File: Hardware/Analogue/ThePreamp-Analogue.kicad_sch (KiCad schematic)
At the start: 32 parts, among them IC1 ULN2803CDWR, J1 To preamp, J14 Conn_01x03_Pin, J15 Conn_02x06_Top_Bottom, J2 From preamp, J3 Digital In, J4 Digital Pass Through, J5 Power In, J6 Power Out, J7 ADS1115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

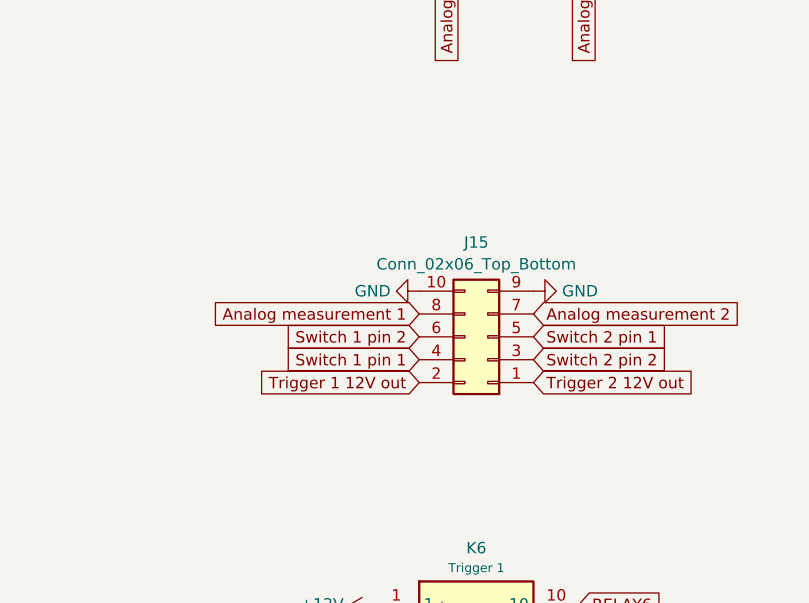
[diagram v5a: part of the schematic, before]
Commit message: Changed switch connector to 1 row
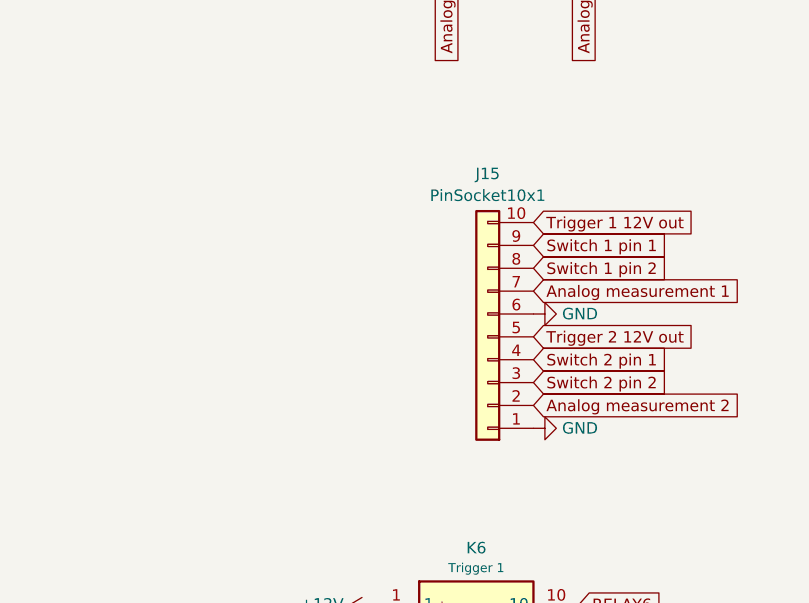
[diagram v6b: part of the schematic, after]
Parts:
- J15: value Conn_02x06_Top_Bottom -> PinSocket10x1; footprint Connector_IDC:IDC-Header_2x05_P2.54mm_Vertical -> Connector_PinSocket_2.54mm:PinSocket_1x10_P2.54mm_Vertical; symbol Connector_Generic:Conn_02x05_Odd_Even -> Connector_Generic:Conn_01x10
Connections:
- net A0: now also J15.7 (Pin_7); no longer J15.8 (Pin_8)
- net A1: now also J15.2 (Pin_2); no longer J15.7 (Pin_7)
- net GND: now also J15.1 (Pin_1), J15.6 (Pin_6); no longer J15.10 (Pin_10), J15.9 (Pin_9)
- net Switch 1 pin 1: now also J15.9 (Pin_9); no longer J15.4 (Pin_4)
- net Switch 1 pin 2: now also J15.8 (Pin_8); no longer J15.6 (Pin_6)
- net Switch 2 pin 1: now also J15.4 (Pin_4); no longer J15.5 (Pin_5)
- net Trigger 1 12V out: now also J15.10 (Pin_10); no longer J15.2 (Pin_2)
- net Trigger 2 12V out: now also J15.5 (Pin_5); no longer J15.1 (Pin_1)
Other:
- moved on the sheet: J15
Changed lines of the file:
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@@
     )
   )
-  (global_label "Analog measurement 2" (shape input) (at 354.076 118.11 0) (fields_autoplaced)
-    (effects (font (size 1.27 1.27)) (justify left))
-    (property "Intersheetrefs" "${INTERSHEET_REFS}" (at 378.5409 118.11 0)
+  (global_label "Analog measurement 2" (shape input) (at 354.076 128.27 0) (fields_autoplaced)
+    (effects (font (size 1.27 1.27)) (justify left))
+    (property "Intersheetrefs" "${INTERSHEET_REFS}" (at 378.5409 128.27 0)
       (effects (font (size 1.27 1.27)) (justify left) hide)
     )
@@
     )
   )
-  (global_label "Switch 1 pin 1" (shape input) (at 341.376 123.19 180) (fields_autoplaced)
-    (effects (font (size 1.27 1.27)) (justify right))
-    (property "Intersheetrefs" "${INTERSHEET_REFS}" (at 324.7123 123.19 0)
-      (effects (font (size 1.27 1.27)) (justify right) hide)
+  (global_label "Switch 1 pin 1" (shape input) (at 354.076 110.49 0) (fields_autoplaced)
+    (effects (font (size 1.27 1.27)) (justify left))
+    (property "Intersheetrefs" "${INTERSHEET_REFS}" (at 370.7397 110.49 0)
+      (effects (font (size 1.27 1.27)) (justify left) hide)
     )
   )
@@
     )
   )
-  (global_label "Trigger 2 12V out" (shape input) (at 354.076 125.73 0) (fields_autoplaced)
-    (effects (font (size 1.27 1.27)) (justify left))
-    (property "Intersheetrefs" "${INTERSHEET_REFS}" (at 373.582 125.73 0)
+  (global_label "Trigger 2 12V out" (shape input) (at 354.076 120.65 0) (fields_autoplaced)
+    (effects (font (size 1.27 1.27)) (justify left))
+    (property "Intersheetrefs" "${INTERSHEET_REFS}" (at 373.582 120.65 0)
       (effects (font (size 1.27 1.27)) (justify left) hide)
     )
@@
     )
   )
-  (global_label "Trigger 1 12V out" (shape input) (at 341.376 125.73 180) (fields_autoplaced)
-    (effects (font (size 1.27 1.27)) (justify right))
-    (property "Intersheetrefs" "${INTERSHEET_REFS}" (at 321.87 125.73 0)
-      (effects (font (size 1.27 1.27)) (justify right) hide)
+  (global_label "Trigger 1 12V out" (shape input) (at 354.076 107.95 0) (fields_autoplaced)
+    (effects (font (size 1.27 1.27)) (justify left))
+    (property "Intersheetrefs" "${INTERSHEET_REFS}" (at 373.582 107.95 0)
+      (effects (font (size 1.27 1.27)) (justify left) hide)
     )
   )
@@
     )
   )
-  (global_label "Switch 2 pin 2" (shape input) (at 354.076 123.19 0) (fields_autoplaced)
-    (effects (font (size 1.27 1.27)) (justify left))
-    (property "Intersheetrefs" "${INTERSHEET_REFS}" (at 370.7397 123.19 0)
+  (global_label "Switch 2 pin 2" (shape input) (at 354.076 125.73 0) (fields_autoplaced)
+    (effects (font (size 1.27 1.27)) (justify left))
+    (property "Intersheetrefs" "${INTERSHEET_REFS}" (at 370.7397 125.73 0)
       (effects (font (size 1.27 1.27)) (justify left) hide)
     )
@@
     )
   )
-  (global_label "Switch 2 pin 1" (shape input) (at 354.076 120.65 0) (fields_autoplaced)
-    (effects (font (size 1.27 1.27)) (justify left))
-    (property "Intersheetrefs" "${INTERSHEET_REFS}" (at 370.7397 120.65 0)
+  (global_label "Switch 2 pin 1" (shape input) (at 354.076 123.19 0) (fields_autoplaced)
+    (effects (font (size 1.27 1.27)) (justify left))
+    (property "Intersheetrefs" "${INTERSHEET_REFS}" (at 370.7397 123.19 0)
       (effects (font (size 1.27 1.27)) (justify left) hide)
     )
@@
     )
   )
-  (global_label "Switch 1 pin 2" (shape input) (at 341.376 120.65 180) (fields_autoplaced)
-    (effects (font (size 1.27 1.27)) (justify right))
-    (property "Intersheetrefs" "${INTERSHEET_REFS}" (at 324.7123 120.65 0)
-      (effects (font (size 1.27 1.27)) (justify right) hide)
+  (global_label "Switch 1 pin 2" (shape input) (at 354.076 113.03 0) (fields_autoplaced)
+    (effects (font (size 1.27 1.27)) (justify left))
+    (property "Intersheetrefs" "${INTERSHEET_REFS}" (at 370.7397 113.03 0)
+      (effects (font (size 1.27 1.27)) (justify left) hide)
     )
   )
@@
     )
   )
-  (global_label "Analog measurement 1" (shape input) (at 341.376 118.11 180) (fields_autoplaced)
-    (effects (font (size 1.27 1.27)) (justify right))
-    (property "Intersheetrefs" "${INTERSHEET_REFS}" (at 316.9111 118.11 0)
-      (effects (font (size 1.27 1.27)) (justify right) hide)
+  (global_label "Analog measurement 1" (shape input) (at 354.076 115.57 0) (fields_autoplaced)
+    (effects (font (size 1.27 1.27)) (justify left))
+    (property "Intersheetrefs" "${INTERSHEET_REFS}" (at 378.5409 115.57 0)
+      (effects (font (size 1.27 1.27)) (justify left) hide)
     )
   )
@@
     )
   )
-  (symbol (lib_id "Connector_Generic:Conn_02x05_Odd_Even") (at 348.996 120.65 180) (unit 1)
-    (in_bom yes) (on_board yes) (dnp no) (fields_autoplaced)
-    (property "Reference" "J15" (at 347.726 110.1557 0)
-      (effects (font (size 1.27 1.27)))
-    )
-    (property "Value" "Conn_02x06_Top_Bottom" (at 347.726 112.5799 0)
-      (effects (font (size 1.27 1.27)))
-    )
-    (property "Footprint" "Connector_IDC:IDC-Header_2x05_P2.54mm_Vertical" (at 348.996 120.65 0)
+  (symbol (lib_id "Connector_Generic:Conn_01x10") (at 348.996 120.65 180) (unit 1)
+    (in_bom yes) (on_board yes) (dnp no) (fields_autoplaced)
+    (property "Reference" "J15" (at 348.996 102.5357 0)
+      (effects (font (size 1.27 1.27)))
+    )
+    (property "Value" "PinSocket10x1" (at 348.996 104.9599 0)
+      (effects (font (size 1.27 1.27)))
+    )
+    (property "Footprint" "Connector_PinSocket_2.54mm:PinSocket_1x10_P2.54mm_Vertical" (at 348.996 120.65 0)
       (effects (font (size 1.27 1.27)) hide)
     )
@@
     )
   )
-  (symbol (lib_id "power:GND") (at 341.376 115.57 270) (unit 1)
+  (symbol (lib_id "power:GND") (at 354.076 118.11 90) (unit 1)
     (in_bom yes) (on_board yes) (dnp no)
-    (property "Reference" "#PWR041" (at 335.026 115.57 0)
-      (effects (font (size 1.27 1.27)) hide)
-    )
-    (property "Value" "GND" (at 338.201 115.57 90)
+    (property "Reference" "#PWR041" (at 360.426 118.11 0)
+      (effects (font (size 1.27 1.27)) hide)
+    )
+    (property "Value" "GND" (at 357.251 118.11 90)
       (effects (font (size 1.27 1.27)) (justify right))
     )
-    (property "Footprint" "" (at 341.376 115.57 0)
-      (effects (font (size 1.27 1.27)) hide)
-    )
-    (property "Datasheet" "" (at 341.376 115.57 0)
+    (property "Footprint" "" (at 354.076 118.11 0)
+      (effects (font (size 1.27 1.27)) hide)
+    )
+    (property "Datasheet" "" (at 354.076 118.11 0)
       (effects (font (size 1.27 1.27)) hide)
     )
@@
     )
   )
-  (symbol (lib_id "power:GND") (at 354.076 115.57 90) (unit 1)
-    (in_bom yes) (on_board yes) (dnp no) (fields_autoplaced)
-    (property "Reference" "#PWR030" (at 360.426 115.57 0)
-      (effects (font (size 1.27 1.27)) hide)
-    )
-    (property "Value" "GND" (at 357.251 115.57 90)
+  (symbol (lib_id "power:GND") (at 354.076 130.81 90) (unit 1)
+    (in_bom yes) (on_board yes) (dnp no)
+    (property "Reference" "#PWR030" (at 360.426 130.81 0)
+      (effects (font (size 1.27 1.27)) hide)
+    )
+    (property "Value" "GND" (at 357.251 130.81 90)
       (effects (font (size 1.27 1.27)) (justify right))
     )
-    (property "Footprint" "" (at 354.076 115.57 0)
-      (effects (font (size 1.27 1.27)) hide)
-    )
-    (property "Datasheet" "" (at 354.076 115.57 0)
-      (effects (font (size 1.27 1.27)) hide)
-    )
+    (property "Footprint" "" (at 354.076 130.81 0)
+      (effects (font (size 1.27 1.27)) hide)
+    )
+    (property "Datasheet" "" (at 354.076 130.81 0)
+      (effects (font (size 1.27 1.27)) hide)
+    )

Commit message: 16 pin IDC connector added for digital control input (GND interleaved)
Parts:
- J15: value PinSocket10x1 -> Switch & trigger outputs and analog inputs
- J3: footprint Connector_JST:JST_XH_B8B-XH-A_1x08_P2.50mm_Vertical -> Connector_IDC:IDC-Header_2x08_P2.54mm_Vertical; symbol Connector:Conn_01x08_Female -> Connector_Generic_MountingPin:Conn_02x08_Odd_Even_MountingPin
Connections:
- net +3.3V: now also J3.10 (Pin_10), J3.6 (Pin_6), J3.7 (Pin_7); no longer J3.4 (Pin_4)
- net GND: now also J3.12 (Pin_12), J3.14 (Pin_14), J3.16 (Pin_16), J3.2 (Pin_2), J3.4 (Pin_4), J3.5 (Pin_5), J3.8 (Pin_8); no longer J3.3 (Pin_3)
- net I2C:SCL: now also J3.3 (Pin_3); no longer J3.2 (Pin_2)
- net SPI:MISO: now also J3.11 (Pin_11); no longer J3.6 (Pin_6)
- net SPI:MOSI: now also J3.13 (Pin_13); no longer J3.7 (Pin_7)
- net SPI:SCK: now also J3.9 (Pin_9); no longer J3.5 (Pin_5)
- net SPI:SS: now also J3.15 (Pin_15); no longer J3.8 (Pin_8)
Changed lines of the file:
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@@
   (junction (at 262.382 71.12) (diameter 0) (color 0 0 0 0)
+  )
+  (junction (at 128.27 228.092) (diameter 0) (color 0 0 0 0)
+  )
+  (junction (at 128.27 238.252) (diameter 0) (color 0 0 0 0)
+  )
+  (junction (at 128.27 223.012) (diameter 0) (color 0 0 0 0)
+  )
+  (junction (at 131.318 225.552) (diameter 0) (color 0 0 0 0)
+  )
+  (junction (at 128.27 235.712) (diameter 0) (color 0 0 0 0)
+  )
+  (junction (at 128.27 233.172) (diameter 0) (color 0 0 0 0)
   )
   (no_connect (at 63.5 117.094))
@@
     (stroke (width 0) (type default))
   )
+  (wire (pts (xy 131.318 230.632) (xy 131.318 225.552))
+    (stroke (width 0) (type default))
+  )
   (wire (pts (xy 262.382 73.66) (xy 261.112 73.66))
     (stroke (width 0) (type default))
   )
+  (wire (pts (xy 128.27 220.472) (xy 128.27 223.012))
+    (stroke (width 0) (type default))
+  )
   (wire (pts (xy 86.614 200.66) (xy 99.06 200.66))
     (stroke (width 0) (type default))
@@
     (stroke (width 0) (type default))
   )
+  (wire (pts (xy 131.064 238.252) (xy 128.27 238.252))
+    (stroke (width 0) (type default))
+  )
   (wire (pts (xy 86.106 166.37) (xy 113.284 166.37))
     (stroke (width 0) (type default))
   )
+  (wire (pts (xy 128.27 233.172) (xy 128.27 235.712))
+    (stroke (width 0) (type default))
+  )
   (wire (pts (xy 110.998 171.45) (xy 113.284 171.45))
     (stroke (width 0) (type default))
@@
     (stroke (width 0) (type default))
   )
+  (wire (pts (xy 128.27 228.092) (xy 128.27 233.172))
+    (stroke (width 0) (type default))
+  )
+  (wire (pts (xy 125.73 233.172) (xy 128.27 233.172))
+    (stroke (width 0) (type default))
+  )
   (wire (pts (xy 86.36 85.344) (xy 97.028 85.344))
     (stroke (width 0) (type default))
@@
     (stroke (width 0) (type default))
   )
+  (wire (pts (xy 125.73 230.632) (xy 131.318 230.632))
+    (stroke (width 0) (type default))
+  )
   (wire (pts (xy 101.854 168.91) (xy 113.284 168.91))
     (stroke (width 0) (type default))
@@
     (stroke (width 0) (type default))
   )
+  (wire (pts (xy 125.73 223.012) (xy 128.27 223.012))
+    (stroke (width 0) (type default))
+  )
   (wire (pts (xy 49.53 200.66) (xy 63.754 200.66))
     (stroke (width 0) (type default))
@@
     (stroke (width 0) (type default))
   )
+  (wire (pts (xy 128.27 235.712) (xy 128.27 238.252))
+    (stroke (width 0) (type default))
+  )
   (wire (pts (xy 86.36 112.014) (xy 97.028 112.014))
     (stroke (width 0) (type default))
   )
+  (wire (pts (xy 125.73 220.472) (xy 128.27 220.472))
+    (stroke (width 0) (type default))
+  )
+  (wire (pts (xy 125.73 235.712) (xy 128.27 235.712))
+    (stroke (width 0) (type default))
+  )
+  (wire (pts (xy 128.27 223.012) (xy 128.27 228.092))
+    (stroke (width 0) (type default))
+  )
+  (wire (pts (xy 128.27 238.252) (xy 125.73 238.252))
+    (stroke (width 0) (type default))
+  )
   (wire (pts (xy 335.534 59.69) (xy 359.664 59.69))
     (stroke (width 0) (type default))
@@
   )
   (wire (pts (xy 230.632 78.74) (xy 230.632 83.82))
+    (stroke (width 0) (type default))
+  )
+  (wire (pts (xy 125.73 228.092) (xy 128.27 228.092))
+    (stroke (width 0) (type default))
+  )
+  (wire (pts (xy 125.73 225.552) (xy 131.318 225.552))
     (stroke (width 0) (type default))
   )
@@
     )
   )
-  (symbol (lib_id "power:GND") (at 113.03 225.552 270) (unit 1)
-    (in_bom yes) (on_board yes) (dnp no)
-    (property "Reference" "#PWR034" (at 106.68 225.552 0)
-      (effects (font (size 1.27 1.27)) hide)
-    )
-    (property "Value" "GND" (at 109.7788 225.679 90)
-      (effects (font (size 1.27 1.27)) (justify right))
-    )
-    (property "Footprint" "" (at 113.03 225.552 0)
-      (effects (font (size 1.27 1.27)) hide)
-    )
-    (property "Datasheet" "" (at 113.03 225.552 0)
-      (effects (font (size 1.27 1.27)) hide)
-    )
-    (pin "1")
-    (instances
-      (project "ThePreamp-Analogue"
-        (path "/f6c644f4-3036-41a6-9e14-2c08c079c6cd"
-          (reference "#PWR034") (unit 1)
-        )
-      )
-    )
-  )
   (symbol (lib_id "power:+12V") (at 63.5 133.35 90) (unit 1)
     (in_bom yes) (on_board yes) (dnp no) (fields_autoplaced)
@@
       (effects (font (size 1.27 1.27)))
     )
-    (property "Value" "PinSocket10x1" (at 348.996 104.9599 0)
+    (property "Value" "Switch & trigger outputs and analog inputs" (at 348.996 104.9599 0)
       (effects (font (size 1.27 1.27)))
     )
@@
     )
   )
+  (symbol (lib_id "power:GND") (at 113.03 225.552 270) (unit 1)
+    (in_bom yes) (on_board yes) (dnp no)
+    (property "Reference" "#PWR027" (at 106.68 225.552 0)
+      (effects (font (size 1.27 1.27)) hide)
+    )
+    (property "Value" "GND" (at 109.7788 225.679 90)
+      (effects (font (size 1.27 1.27)) (justify right))
+    )
+    (property "Footprint" "" (at 113.03 225.552 0)
+      (effects (font (size 1.27 1.27)) hide)
+    )
+    (property "Datasheet" "" (at 113.03 225.552 0)
+      (effects (font (size 1.27 1.27)) hide)
+    )
+    (pin "1")
+    (instances
+      (project "ThePreamp-Analogue"
+        (path "/f6c644f4-3036-41a6-9e14-2c08c079c6cd"
+          (reference "#PWR027") (unit 1)
+        )
+      )
+    )
+  )
   (symbol (lib_id "power:GNDA") (at 102.108 117.094 0) (unit 1)
     (in_bom yes) (on_board yes) (dnp no) (fields_autoplaced)
@@
     )
   )
-  (symbol (lib_id "Connector:Conn_01x08_Female") (at 118.11 228.092 0) (unit 1)
+  (symbol (lib_id "Connector_Generic_MountingPin:Conn_02x08_Odd_Even_MountingPin") (at 118.11 228.092 0) (unit 1)
     (in_bom yes) (on_board yes) (dnp no)
-    (property "Reference" "J3" (at 123.19 227.33 0)
+    (property "Reference" "J3" (at 117.094 213.106 0)
       (effects (font (size 1.27 1.27)) (justify right))
     )
-    (property "Value" "Digital In" (at 129.54 231.14 0)
+    (property "Value" "Digital In" (at 123.444 216.916 0)
       (effects (font (size 1.27 1.27)) (justify right))
     )
-    (property "Footprint" "Connector_JST:JST_XH_B8B-XH-A_1x08_P2.50mm_Vertical" (at 118.11 228.092 0)
+    (property "Footprint" "Connector_IDC:IDC-Header_2x08_P2.54mm_Vertical" (at 118.11 228.092 0)
       (effects (font (size 1.27 1.27)) hide)
     )
@@
     (pin "7")
     (pin "8")
+    (pin "15")
+    (pin "14")
+    (pin "16")
+    (pin "13")
+    (pin "11")
+    (pin "MP")
+    (pin "12")
+    (pin "9")
+    (pin "10")
     (instances
       (project "ThePreamp-Analogue"
@@
   (symbol (lib_id "power:+3.3V") (at 113.03 228.092 90) (unit 1)
     (in_bom yes) (on_board yes) (dnp no) (fields_autoplaced)
-    (property "Reference" "#PWR037" (at 116.84 228.092 0)
+    (property "Reference" "#PWR012" (at 116.84 228.092 0)
       (effects (font (size 1.27 1.27)) hide)
     )
@@
     )
     (property "Datasheet" "" (at 113.03 228.092 0)
+      (effects (font (size 1.27 1.27)) hide)
+    )
+    (pin "1")
+    (instances
+      (project "ThePreamp-Analogue"
+        (path "/f6c644f4-3036-41a6-9e14-2c08c079c6cd"
+          (reference "#PWR012") (unit 1)
+        )
+      )
+    )
+  )
+  (symbol (lib_id "power:+3.3V") (at 131.318 225.552 270) (unit 1)
+    (in_bom yes) (on_board yes) (dnp no) (fields_autoplaced)
+    (property "Reference" "#PWR037" (at 127.508 225.552 0)
+      (effects (font (size 1.27 1.27)) hide)
+    )
+    (property "Value" "+3.3V" (at 134.493 225.552 90)
+      (effects (font (size 1.27 1.27)) (justify left))
+    )
+    (property "Footprint" "" (at 131.318 225.552 0)
+      (effects (font (size 1.27 1.27)) hide)
+    )
+    (property "Datasheet" "" (at 131.318 225.552 0)
       (effects (font (size 1.27 1.27)) hide)
     )
@@
         )
       )
+    )
+  )
+  (symbol (lib_id "power:GND") (at 131.064 238.252 90) (unit 1)
+    (in_bom yes) (on_board yes) (dnp no)
+    (property "Reference" "#PWR011" (at 137.414 238.252 0)
+      (effects (font (size 1.27 1.27)) hide)
+    )
+    (property "Value" "GND" (at 134.3152 238.125 90)
+      (effects (font (size 1.27 1.27)) (justify right))
+    )
+    (property "Footprint" "" (at 131.064 238.252 0)
+      (effects (font (size 1.27 1.27)) hide)
+    )
+    (property "Datasheet" "" (at 131.064 238.252 0)
+      (effects (font (size 1.27 1.27)) hide)
+    )
+    (pin "1")
+    (instances
+      (project "ThePreamp-Analogue"
+        (path "/f6c644f4-3036-41a6-9e14-2c08c079c6cd"
+          (reference "#PWR011") (unit 1)
+        )
+      )
